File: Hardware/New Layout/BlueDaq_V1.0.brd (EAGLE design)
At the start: 69 x 75 mm, 72 parts, among them IC1 MEGA8-AI, Q1 MMBT2222, Q2 MMBT2222, Q3 MMBT2222, Q4 MMBT2222, U1 MCP73831, U2 TPS61200, U3 BME280, U4 MIC5225-3.3, U5 MIC5219 5V, X1 USB-MICROB, X2 3.5mm, X4 3.5mm, Y1 16 mhz

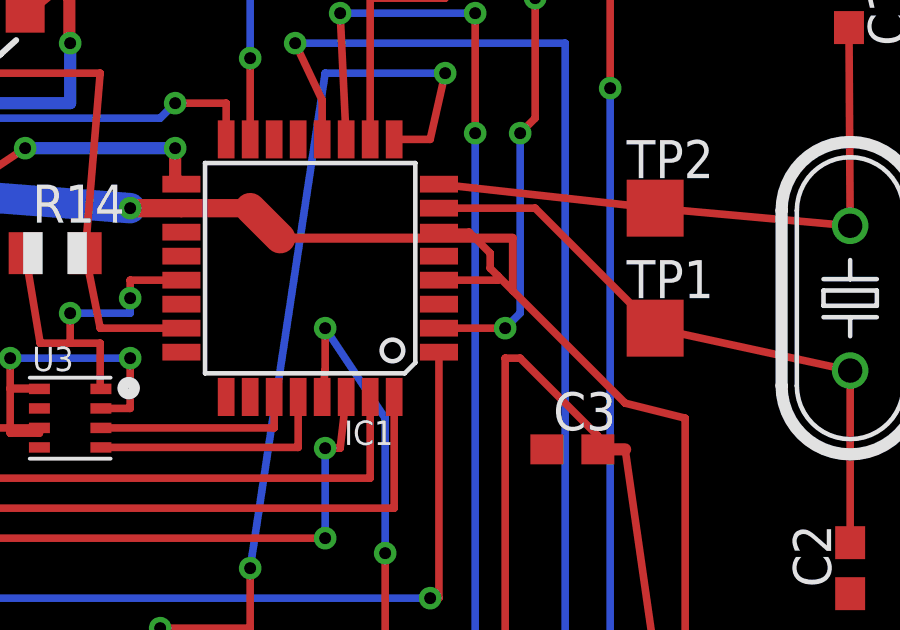
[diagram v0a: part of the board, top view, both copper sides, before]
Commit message: More fat traces
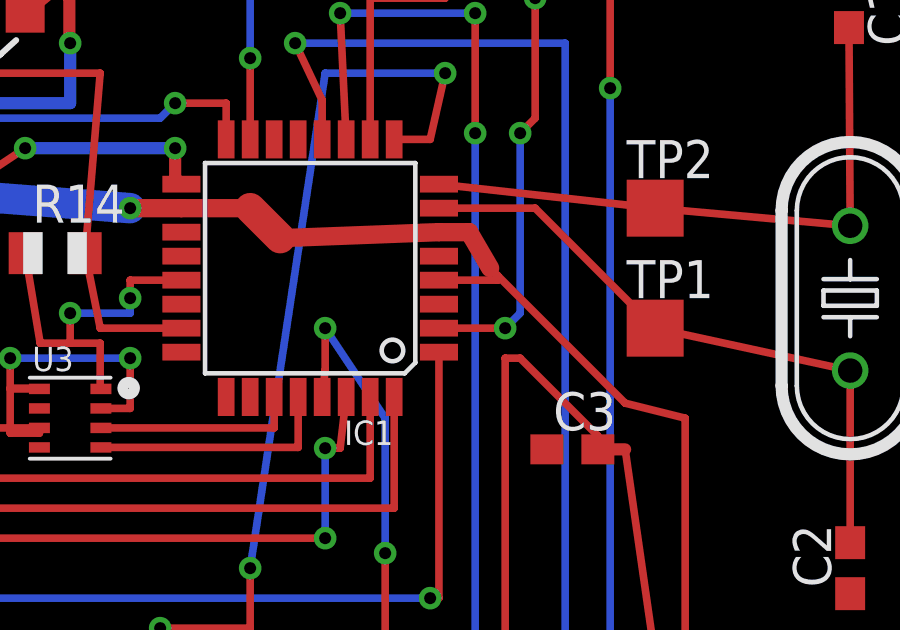
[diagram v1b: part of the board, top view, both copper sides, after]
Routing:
- net VCC: track 207.2 -> 202.9 mm
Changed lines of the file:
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@@
 <wire x1="60.5" y1="32" x2="60.5" y2="42" width="0.254" layer="1"/>
 <wire x1="60.5" y1="42" x2="58.5" y2="42.5" width="0.254" layer="1"/>
-<wire x1="58.5" y1="42.5" x2="54.75" y2="46.25" width="0.254" layer="1"/>
-<wire x1="54.75" y1="46.25" x2="54.25" y2="46.75" width="0.254" layer="1"/>
+<wire x1="58.5" y1="42.5" x2="54.25" y2="46.75" width="0.254" layer="1"/>
 <wire x1="54.25" y1="46.75" x2="54" y2="47" width="0.254" layer="1"/>
 <wire x1="27.66" y1="36.5" x2="30" y2="36.5" width="0.254" layer="1"/>
@@
 <wire x1="43.7074" y1="49" x2="46" y2="49" width="0.6096" layer="1"/>
 <wire x1="46" y1="49" x2="47" y2="48" width="1.016" layer="1"/>
-<wire x1="47" y1="48" x2="54.75" y2="48" width="0.3048" layer="1"/>
 <contactref element="IC1" pad="6"/>
 <contactref element="IC1" pad="4"/>
@@
 <wire x1="6" y1="30.5" x2="2" y2="30.5" width="0.254" layer="1"/>
 <wire x1="2" y1="30.5" x2="2" y2="30.19" width="0.254" layer="1"/>
-<wire x1="54" y1="47" x2="54" y2="47.5" width="0.254" layer="1"/>
-<wire x1="54" y1="47.5" x2="53.3" y2="48.2" width="0.254" layer="1"/>
-<wire x1="53.3" y1="48.2" x2="52.2926" y2="48.2" width="0.254" layer="1"/>
+<wire x1="53.3" y1="48.2" x2="52.2926" y2="48.2" width="0.6096" layer="1"/>
 <wire x1="52.2926" y1="46.6" x2="54.25" y2="46.6" width="0.254" layer="1"/>
 <wire x1="54.25" y1="46.6" x2="54.25" y2="46.75" width="0.254" layer="1"/>
-<wire x1="54.75" y1="48" x2="54.75" y2="46.25" width="0.254" layer="1"/>
+<wire x1="47" y1="48" x2="52.2926" y2="48.2" width="0.6096" layer="1"/>
+<wire x1="53.3" y1="48.2" x2="54" y2="47" width="0.6096" layer="1"/>
 </signal>
 <signal name="GND">

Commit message: + Minor Changes to Schematic
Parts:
- removed C3: 1u, rcl:C0603
- added D8: (no value), adafruit:SMADIODE
- C12: value 0.1uF -> 10uF
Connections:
- removed net BT_DTR: C3.1
- removed net N$21: R22.1, U5.5
- new net N$18: D8.C, R22.1
- new net N$5: D8.A, U5.5
- net RESET_PIN: no longer C3.2
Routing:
- net N$21: track 10.7 -> 0.00 mm
- net RESET_PIN: track 84.8 -> 83.4 mm
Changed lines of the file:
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@@
 <?xml version="1.0" encoding="utf-8"?>
 <!DOCTYPE eagle SYSTEM "eagle.dtd">
-<eagle version="7.6.0">
+<eagle version="7.7.0">
 <drawing>
 <settings>
@@
 <element name="C1" library="rcl" package="C0603" value="22p" x="65.96" y="55.87" rot="R270"/>
 <element name="C10" library="SparkFun" package="0402-CAP" value="4.7uF" x="52" y="64" rot="R90"/>
-<element name="C12" library="microbuilder" package="0805-NO@1" value="0.1uF" x="29" y="62"/>
+<element name="C12" library="microbuilder" package="0805-NO@1" value="10uF" x="29" y="62"/>
 <element name="C13" library="microbuilder" package="0805-NO@1" value="0.1uF" x="17" y="53.5"/>
 <element name="C2" library="rcl" package="C0603" value="22p" x="66" y="37" rot="R90"/>
-<element name="C3" library="rcl" package="C0603" value="1u" x="56.74" y="40.96"/>
 <element name="C4" library="CH_passive" package="0805" value="22uF" x="42.96" y="61.23" rot="R90"/>
 <element name="C5" library="SparkFun" package="0402-CAP" value="0.1uF" x="32" y="60" rot="R180"/>
@@
 <element name="C11" library="microbuilder" package="0805-NO@1" value="0.1uF" x="17.5" y="31" rot="R90"/>
 <element name="BT" library="adafruit" package="1X06" value="" x="2" y="34" rot="R270"/>
+<element name="D8" library="adafruit" package="SMADIODE" value="" x="1" y="-6.5"/>
 </elements>
 <signals>
@@
 </signal>
 <signal name="RESET_PIN">
-<contactref element="C3" pad="2"/>
 <contactref element="IC1" pad="29"/>
 <contactref element="R1" pad="1"/>
@@
 <wire x1="29.99" y1="44.46" x2="25.2" y2="49.25" width="0.4064" layer="1"/>
 <wire x1="59.5" y1="34" x2="58.5" y2="40.96" width="0.254" layer="1"/>
-<wire x1="58.5" y1="40.96" x2="57.59" y2="40.96" width="0.4064" layer="1"/>
-<wire x1="57.59" y1="40.96" x2="57.59" y2="41.41" width="0.254" layer="1"/>
 <wire x1="57.59" y1="41.41" x2="55" y2="44" width="0.254" layer="1"/>
 <wire x1="55" y1="44" x2="54.5" y2="44" width="0.254" layer="1"/>
@@
 <via x="50.5" y="37.5" extent="1-16" drill="0.4"/>
 <wire x1="50.5" y1="37.5" x2="50.5" y2="34" width="0.254" layer="1"/>
+<wire x1="57.59" y1="41.41" x2="58.5" y2="40.96" width="0" layer="19" extent="1-1"/>
 </signal>
 <signal name="VBATT">
@@
 <via x="34.5" y="64" extent="1-16" drill="0.4"/>
 <wire x1="34.5" y1="64" x2="36" y2="64.475" width="0.254" layer="1"/>
-</signal>
-<signal name="BT_DTR">
-<contactref element="C3" pad="1"/>
 </signal>
 <signal name="SDA">
@@
 <wire x1="13.05" y1="66.3001" x2="19.05" y2="66.3001" width="0.4064" layer="1"/>
 </signal>
-<signal name="N$21">
-<contactref element="U5" pad="5"/>
-<contactref element="R22" pad="1"/>
-<wire x1="23.05" y1="62.3001" x2="23.05" y2="68" width="0.4064" layer="1"/>
-<wire x1="23.05" y1="68" x2="22" y2="68" width="0.4064" layer="1"/>
-<wire x1="22" y1="68" x2="22" y2="70" width="0.4064" layer="1"/>
-<wire x1="22" y1="70" x2="20" y2="70" width="0.4064" layer="1"/>
-</signal>
 <signal name="N$23">
 <contactref element="C9" pad="1"/>
@@
 <wire x1="60.5" y1="69.93" x2="60.63" y2="69.93" width="0.4064" layer="1"/>
 </signal>
+<signal name="N$5">
+<contactref element="U5" pad="5"/>
+<contactref element="D8" pad="A"/>
+<wire x1="3.3495" y1="-6.5" x2="23.05" y2="62.3001" width="0" layer="19" extent="1-1"/>
+</signal>
+<signal name="N$18">
+<contactref element="D8" pad="C"/>
+<contactref element="R22" pad="1"/>
+<wire x1="-1.3495" y1="-6.5" x2="20" y2="70" width="0" layer="19" extent="1-1"/>
+</signal>
 </signals>

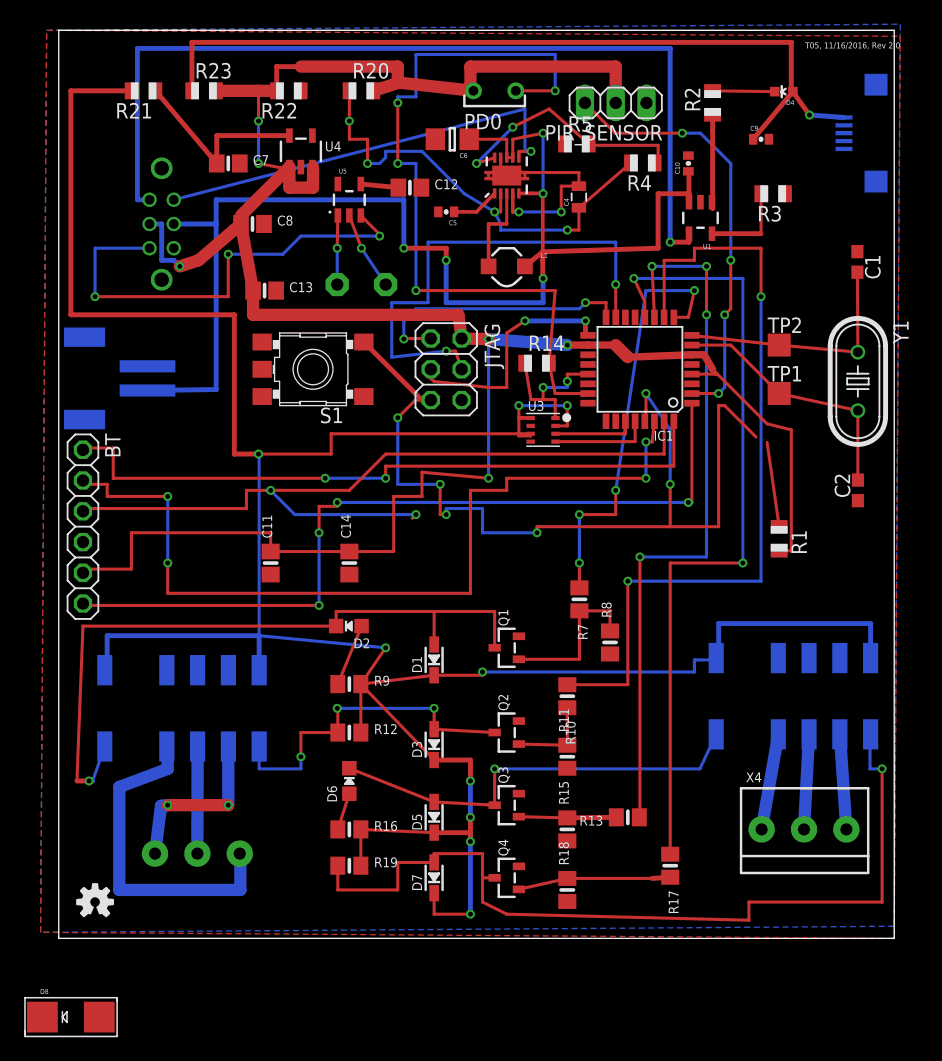
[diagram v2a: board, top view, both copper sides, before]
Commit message: added new diode
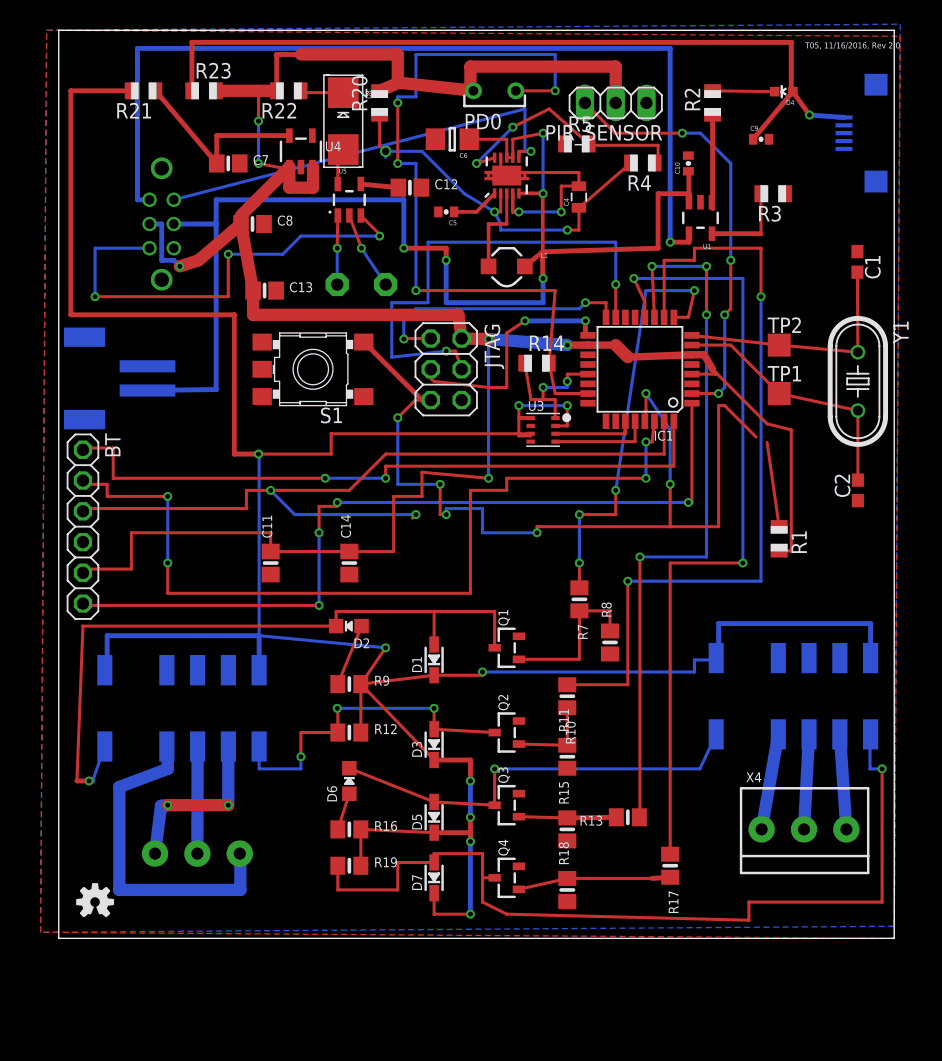
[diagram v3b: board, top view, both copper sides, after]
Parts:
- moved D8 77.3 mm to (23.5, 67.5), turned to 270 degrees
- moved R20 1.80 mm to (26.5, 69.0), turned to 90 degrees
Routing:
- net N$20: track 38.2 -> 32.2 mm, vias 4 -> 3
- net N$18: track 0.00 -> 3.65 mm
- net N$5: track 0.00 -> 3.30 mm
- net VCC: track 202.9 -> 204.4 mm
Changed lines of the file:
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@@
 <?xml version="1.0" encoding="utf-8"?>
 <!DOCTYPE eagle SYSTEM "eagle.dtd">
-<eagle version="7.7.0">
+<eagle version="7.6.0">
 <drawing>
 <settings>
@@
 <element name="R19" library="microbuilder" package="0805-NO" value="1K" x="24" y="6"/>
 <element name="R2" library="adafruit" package="R0805" value="470" x="54" y="69" rot="R90"/>
-<element name="R20" library="adafruit" package="R0805" value="0" x="25" y="70"/>
+<element name="R20" library="adafruit" package="R0805" value="0" x="26.5" y="69" rot="R90"/>
 <element name="R21" library="adafruit" package="R0805" value="0" x="7" y="70" rot="R180"/>
 <element name="R22" library="adafruit" package="R0805" value="0" x="19" y="70" rot="R180"/>
@@
 <element name="C11" library="microbuilder" package="0805-NO@1" value="0.1uF" x="17.5" y="31" rot="R90"/>
 <element name="BT" library="adafruit" package="1X06" value="" x="2" y="34" rot="R270"/>
-<element name="D8" library="adafruit" package="SMADIODE" value="" x="1" y="-6.5"/>
+<element name="D8" library="adafruit" package="SMADIODE" value="" x="23.5" y="67.5" rot="R270"/>
 </elements>
 <signals>
@@
 <contactref element="C13" pad="1"/>
 <wire x1="34.25" y1="70" x2="28.1045" y2="70.673440625" width="1.016" layer="1"/>
-<wire x1="28.1045" y1="70.673440625" x2="26" y2="70" width="1.016" layer="1"/>
-<wire x1="20" y1="72" x2="28" y2="72" width="1.016" layer="1"/>
-<wire x1="28" y1="72" x2="28" y2="70.673440625" width="1.016" layer="1"/>
+<wire x1="28.1045" y1="70.673440625" x2="26.5" y2="70" width="1.016" layer="1"/>
+<wire x1="20" y1="73" x2="28" y2="73" width="1.016" layer="1"/>
+<wire x1="28" y1="73" x2="28" y2="70.673440625" width="1.016" layer="1"/>
 <wire x1="28" y1="70.673440625" x2="28.1045" y2="70.673440625" width="0.254" layer="1"/>
-<wire x1="20" y1="72" x2="18" y2="72" width="0.4064" layer="1"/>
-<wire x1="18" y1="72" x2="18" y2="70" width="0.4064" layer="1"/>
+<wire x1="20" y1="73" x2="18" y2="73" width="0.4064" layer="1"/>
+<wire x1="18" y1="73" x2="18" y2="70" width="0.4064" layer="1"/>
 <wire x1="18" y1="70" x2="16.5" y2="70" width="1.016" layer="1"/>
 <wire x1="16.5" y1="70" x2="13" y2="70" width="1.016" layer="1"/>
@@
 <via x="36" y="60" extent="1-16" drill="0.4"/>
 <wire x1="36" y1="60" x2="33.5" y2="61.5" width="0.254" layer="16"/>
-<via x="24" y="67.5" extent="1-16" drill="0.4"/>
-<wire x1="24" y1="67.5" x2="24" y2="70" width="0.254" layer="1"/>
 <wire x1="33.5" y1="61.5" x2="30" y2="65" width="0.254" layer="16"/>
 <wire x1="30" y1="65" x2="27" y2="65" width="0.254" layer="16"/>
 <wire x1="27" y1="65" x2="27" y2="64.5" width="0.254" layer="16"/>
-<wire x1="27" y1="64.5" x2="26.5" y2="64" width="0.254" layer="16"/>
-<wire x1="26.5" y1="64" x2="25.5" y2="64" width="0.254" layer="16"/>
-<via x="25.5" y="64" extent="1-16" drill="0.4"/>
-<wire x1="25.5" y1="64" x2="25.5" y2="66" width="0.254" layer="1"/>
-<wire x1="25.5" y1="66" x2="24" y2="66" width="0.254" layer="1"/>
-<wire x1="24" y1="66" x2="24" y2="67.5" width="0.254" layer="1"/>
+<wire x1="26.5" y1="68" x2="26.5" y2="65.5" width="0.254" layer="1"/>
+<wire x1="26.5" y1="65.5" x2="27" y2="65" width="0.254" layer="1"/>
+<via x="27" y="65" extent="1-16" drill="0.6"/>
 </signal>
 <signal name="OUT">
@@
 <contactref element="U5" pad="5"/>
 <contactref element="D8" pad="A"/>
-<wire x1="3.3495" y1="-6.5" x2="23.05" y2="62.3001" width="0" layer="19" extent="1-1"/>
+<wire x1="23.5" y1="65.1505" x2="23.05" y2="65.1505" width="0.254" layer="1"/>
+<wire x1="23.05" y1="65.1505" x2="23.05" y2="62.3001" width="0.254" layer="1"/>
 </signal>
 <signal name="N$18">
 <contactref element="D8" pad="C"/>
 <contactref element="R22" pad="1"/>
-<wire x1="-1.3495" y1="-6.5" x2="20" y2="70" width="0" layer="19" extent="1-1"/>
+<wire x1="23.5" y1="69.8495" x2="20" y2="69.8495" width="0.254" layer="1"/>
+<wire x1="20" y1="69.8495" x2="20" y2="70" width="0.254" layer="1"/>
 </signal>
 </signals>
